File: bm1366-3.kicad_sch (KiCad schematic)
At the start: 77 parts, among them U1 25MHz, U14 BM1366_mode1, U21 TLV3544, U23 AP7331, U24 AP7331

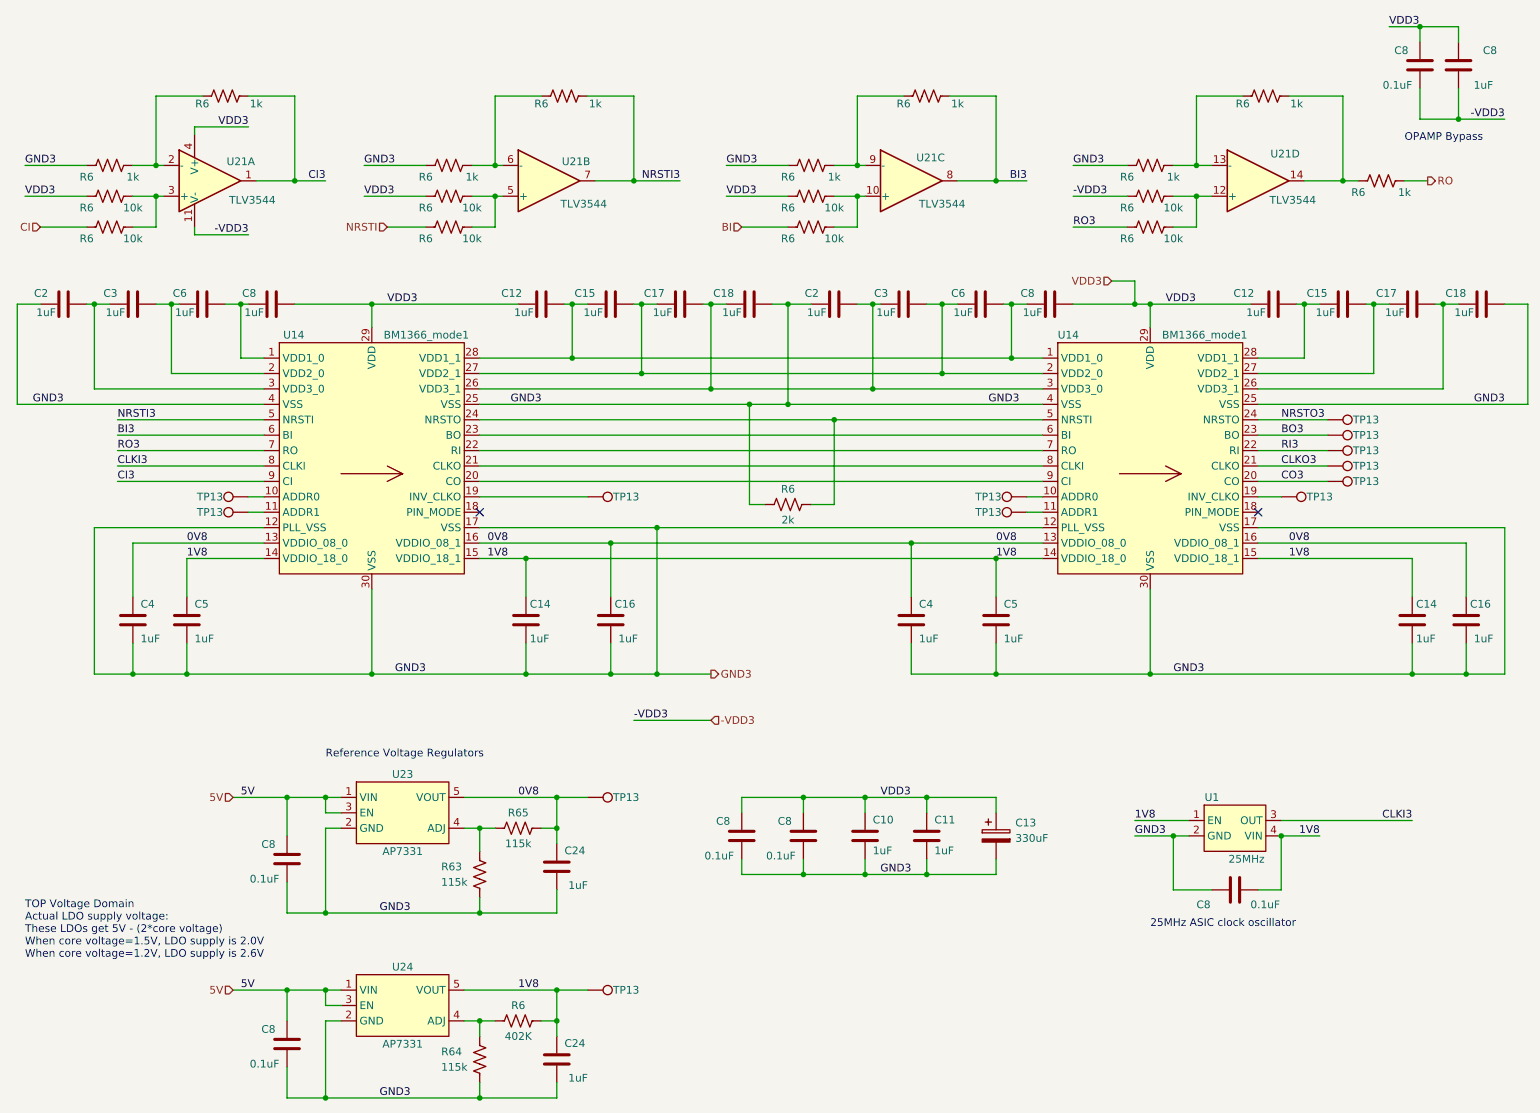
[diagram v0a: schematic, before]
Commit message: finish sch rearrange for BM1368 chain
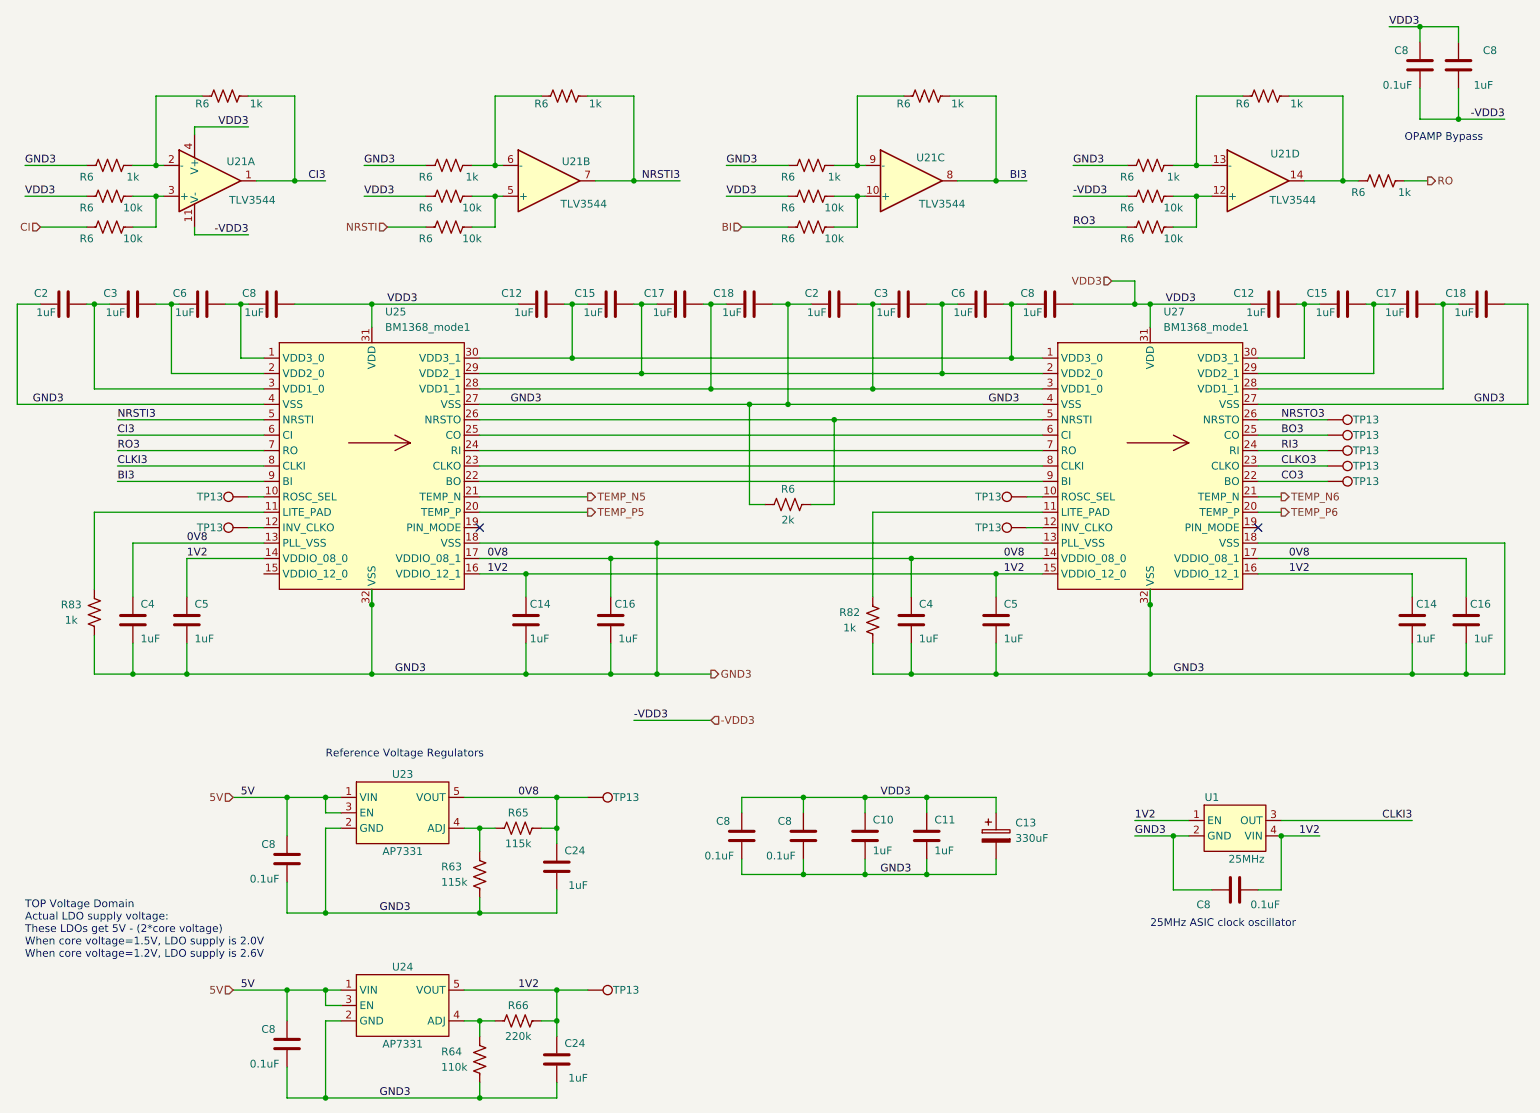
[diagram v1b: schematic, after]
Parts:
- removed R6: 402K, Resistor_SMD:R_0402_1005Metric, symbol Device:R_US
- removed TP13 (x2): TestPoint, TestPoint:TestPoint_Pad_D1.0mm, symbol Connector:TestPoint
- removed U14 (x2): BM1366_mode1, bitaxe:BM1366, symbol bitaxe:BM1366_mode1
- added R66: 220k, Resistor_SMD:R_0402_1005Metric, symbol Device:R_US
- added R82, R83: 1k, Resistor_SMD:R_0402_1005Metric, symbol Device:R_US
- added U25, U27: BM1368_mode1, bitaxe:BM1368, symbol bitaxe:BM1368_mode1
- R64: value 115k -> 110k; DK YAG2956CT-ND -> 311-110KLRTR-ND; PARTNO RC0402FR-07115KL -> RC0402FR-07110KL
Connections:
- net 0V8: now also U25.13 (PLL_VSS), U25.17 (VDDIO_08_1), U27.14 (VDDIO_08_0), U27.17 (VDDIO_08_1)
- net BI3: now also U25.9 (BI)
- net BO3: now also U27.25 (CO)
- net CI3: now also U25.6 (CI)
- net CLKI3: now also U25.8 (CLKI)
- net CLKO3: now also U27.23 (CLKO)
- net CO3: now also U27.22 (BO)
- net GND3: now also R82.1, R83.1, U25.18 (VSS), U25.27 (VSS), U25.32 (VSS), U25.4 (VSS), U27.13 (PLL_VSS), U27.18 (VSS), U27.27 (VSS), U27.32 (VSS), U27.4 (VSS)
- net NRSTI3: now also U25.5 (NRSTI)
- net NRSTO3: now also U27.26 (NRSTO)
- net RI3: now also U27.24 (RI)
- net RO3: now also U25.7 (RO)
- net VDD3: now also U25.31 (VDD), U27.31 (VDD)
- net at C17.2, C18.1: now also U27.28 (VDD1_1)
- net at C12.2, C15.1: now also U27.30 (VDD3_1)
- net at C6.2, C8.1: now also U25.1 (VDD3_0)
- net at C17.2, C18.1, C2.2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: now also U25.28 (VDD1_1), U27.3 (VDD1_0)
- net at C15.2, C17.1, C3.2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: now also U25.29 (VDD2_1), U27.2 (VDD2_0)
- net at R64.2, U24.4 (ADJ): now also R66.2
- net at C12.2, C15.1, C6.2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: now also U25.30 (VDD3_1), U27.1 (VDD3_0)
- net at R6.2: now also U25.26 (NRSTO), U27.5 (NRSTI)
- net at C15.2, C17.1: now also U27.29 (VDD2_1)
- net at C3.2, C6.1: now also U25.2 (VDD2_0)
- net at TP13.1: now also U27.10 (ROSC_SEL)
- net at TP13.1: now also U27.12 (INV_CLKO)
- net at C2.2, C3.1: now also U25.3 (VDD1_0)
- net at TP13.1: now also U25.12 (INV_CLKO)
- net at TP13.1: now also U25.10 (ROSC_SEL)
- net 1V8 renamed 1V2
- net 1V2: now also R66.1, U25.14 (VDDIO_08_0), U25.16 (VDDIO_12_1), U27.15 (VDDIO_12_0), U27.16 (VDDIO_12_1)
- new net: R83.2, U25.11 (LITE_PAD)
- new net: R82.2, U27.11 (LITE_PAD)
- new net: U25.25 (CO), U27.6 (CI)
- new net: U25.24 (RI), U27.7 (RO)
- new net: U25.23 (CLKO), U27.8 (CLKI)
- new net: U25.22 (BO), U27.9 (BI)
- new net TEMP_N5: U25.21 (TEMP_N)
- new net TEMP_N6: U27.21 (TEMP_N)
- new net TEMP_P5: U25.20 (TEMP_P)
- new net TEMP_P6: U27.20 (TEMP_P)
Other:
- moved on the sheet: TP13

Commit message: sch update done
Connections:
- net 0V8: now also U25.14 (VDDIO_08_0); no longer U25.13 (PLL_VSS)
- net 1V2: now also U25.15 (VDDIO_12_0); no longer U25.14 (VDDIO_08_0)
- net GND3: now also U25.13 (PLL_VSS)
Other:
- moved on the sheet: R83
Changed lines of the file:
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@@
 	)
 	(junction
+		(at 30.48 124.46)
+		(diameter 0)
+		(color 0 0 0 0)
+	)
+	(junction
 		(at 66.04 176.53)
 		(diameter 0)
@@
 	(wire
 		(pts
+			(xy 55.88 102.87) (xy 30.48 102.87)
+		)
+		(stroke
+			(width 0)
+			(type default)
+		)
+	)
+	(wire
+		(pts
 			(xy 162.56 124.46) (xy 162.56 119.38)
 		)
@@
 	(wire
 		(pts
+			(xy 30.48 102.87) (xy 30.48 124.46)
+		)
+		(stroke
+			(width 0)
+			(type default)
+		)
+	)
+	(wire
+		(pts
 			(xy 153.67 29.21) (xy 161.29 29.21)
 		)
@@
 	(wire
 		(pts
+			(xy 43.18 107.95) (xy 43.18 111.76)
+		)
+		(stroke
+			(width 0)
+			(type default)
+		)
+	)
+	(wire
+		(pts
 			(xy 167.64 63.5) (xy 170.18 63.5)
 		)
@@
 	(wire
 		(pts
+			(xy 30.48 124.46) (xy 34.29 124.46)
+		)
+		(stroke
+			(width 0)
+			(type default)
+		)
+	)
+	(wire
+		(pts
 			(xy 34.29 50.8) (xy 38.1 50.8)
 		)
@@
 	(wire
 		(pts
-			(xy 43.18 105.41) (xy 55.88 105.41)
-		)
-		(stroke
-			(width 0)
-			(type default)
-		)
-	)
-	(wire
-		(pts
 			(xy 165.1 154.94) (xy 165.1 157.48)
 		)
@@
 	(wire
 		(pts
-			(xy 27.94 97.79) (xy 55.88 97.79)
+			(xy 26.67 97.79) (xy 55.88 97.79)
 		)
 		(stroke
@@
 	(wire
 		(pts
-			(xy 27.94 110.49) (xy 27.94 97.79)
+			(xy 26.67 110.49) (xy 26.67 97.79)
 		)
 		(stroke
@@
 	(wire
 		(pts
-			(xy 31.75 92.71) (xy 55.88 92.71)
+			(xy 34.29 105.41) (xy 55.88 105.41)
 		)
 		(stroke
@@
 	(wire
 		(pts
-			(xy 238.76 74.93) (xy 238.76 63.5)
+			(xy 31.75 92.71) (xy 55.88 92.71)
 		)
 		(stroke
@@
 	(wire
 		(pts
-			(xy 149.86 45.72) (xy 153.67 45.72)
+			(xy 238.76 74.93) (xy 238.76 63.5)
 		)
 		(stroke
@@
 	(wire
 		(pts
-			(xy 195.58 59.69) (xy 199.39 59.69)
+			(xy 149.86 45.72) (xy 153.67 45.72)
 		)
 		(stroke
@@
 	(wire
 		(pts
-			(xy 162.56 124.46) (xy 176.53 124.46)
+			(xy 195.58 59.69) (xy 199.39 59.69)
 		)
 		(stroke
@@
 	(wire
 		(pts
-			(xy 34.29 102.87) (xy 34.29 111.76)
+			(xy 162.56 124.46) (xy 176.53 124.46)
 		)
 		(stroke
@@
 	(wire
 		(pts
-			(xy 27.94 118.11) (xy 27.94 124.46)
+			(xy 26.67 118.11) (xy 26.67 124.46)
 		)
 		(stroke
@@
 	(wire
 		(pts
-			(xy 43.18 105.41) (xy 43.18 111.76)
-		)
-		(stroke
-			(width 0)
-			(type default)
-		)
-	)
-	(wire
-		(pts
 			(xy 252.73 27.94) (xy 252.73 33.02)
 		)
@@
 	(wire
 		(pts
-			(xy 245.11 124.46) (xy 254 124.46)
+			(xy 34.29 105.41) (xy 34.29 111.76)
 		)
 		(stroke
@@
 	(wire
 		(pts
-			(xy 179.07 63.5) (xy 181.61 63.5)
+			(xy 245.11 124.46) (xy 254 124.46)
 		)
 		(stroke
@@
 	(wire
 		(pts
-			(xy 99.06 119.38) (xy 99.06 124.46)
+			(xy 179.07 63.5) (xy 181.61 63.5)
 		)
 		(stroke
@@
 	(wire
 		(pts
-			(xy 76.2 50.8) (xy 82.55 50.8)
+			(xy 99.06 119.38) (xy 99.06 124.46)
 		)
 		(stroke
@@
 	(wire
 		(pts
-			(xy 167.64 74.93) (xy 184.15 74.93)
+			(xy 76.2 50.8) (xy 82.55 50.8)
 		)
 		(stroke
@@
 	(wire
 		(pts
-			(xy 27.94 124.46) (xy 34.29 124.46)
+			(xy 167.64 74.93) (xy 184.15 74.93)
 		)
 		(stroke
@@
 	(wire
 		(pts
-			(xy 19.05 50.8) (xy 26.67 50.8)
+			(xy 26.67 124.46) (xy 30.48 124.46)
 		)
 		(stroke
@@
 	(wire
 		(pts
-			(xy 93.98 29.21) (xy 101.6 29.21)
+			(xy 19.05 50.8) (xy 26.67 50.8)
 		)
 		(stroke
@@
 	(wire
 		(pts
-			(xy 34.29 40.64) (xy 38.1 40.64)
+			(xy 93.98 29.21) (xy 101.6 29.21)
 		)
 		(stroke
@@
 	(wire
 		(pts
-			(xy 34.29 102.87) (xy 55.88 102.87)
+			(xy 34.29 40.64) (xy 38.1 40.64)
 		)
 		(stroke
@@
 	(wire
 		(pts
+			(xy 43.18 107.95) (xy 55.88 107.95)
+		)
+		(stroke
+			(width 0)
+			(type default)
+		)
+	)
+	(wire
+		(pts
 			(xy 59.69 176.53) (xy 66.04 176.53)
 		)
@@
 	)
 	(label "1V2"
-		(at 43.18 105.41 0)
+		(at 49.53 107.95 0)
 		(fields_autoplaced yes)
 		(effects
@@
 	)
 	(label "0V8"
-		(at 43.18 102.87 0)
+		(at 49.53 105.41 0)
 		(fields_autoplaced yes)
 		(effects
@@
 	(symbol
 		(lib_id "Device:R_US")
-		(at 27.94 114.3 180)
+		(at 26.67 114.3 180)
 		(unit 1)
 		(exclude_from_sim no)
@@
 		(dnp no)
 		(property "Reference" "R83"
-			(at 24.13 113.03 0)
+			(at 22.86 113.03 0)
 			(effects
 				(font
@@
 		)
 		(property "Value" "1k"
-			(at 24.13 115.57 0)
+			(at 22.86 115.57 0)
 			(effects
 				(font
@@
 		)
 		(property "Footprint" "Resistor_SMD:R_0402_1005Metric"
-			(at 26.924 114.046 90)
+			(at 25.654 114.046 90)
 			(effects
 				(font
@@
 		)
 		(property "Datasheet" "~"
-			(at 27.94 114.3 0)
+			(at 26.67 114.3 0)
 			(effects
 				(font
@@
 		)
 		(property "Description" ""
-			(at 27.94 114.3 0)
+			(at 26.67 114.3 0)
 			(effects
 				(font
@@
 		)
 		(property "DK" "311-1.00KLRCT-ND"
-			(at 27.94 114.3 0)
+			(at 26.67 114.3 0)
 			(effects
 				(font
@@
 		)
 		(property "PARTNO" "RC0402FR-071KL"
-			(at 27.94 114.3 0)
+			(at 26.67 114.3 0)
 			(effects
 				(font
